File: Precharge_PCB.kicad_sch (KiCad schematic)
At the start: 74 parts, among them J1 Conn_01x02, J10 Conn_01x06, J2 Conn_01x02, J3 Conn_01x08, J4 Conn_01x02, J5 Conn_01x03, J9 Conn_01x02, K1 G2RL-1A, K2 G2RL-1A, Q1 DMN61D8LQ, Q2 DMN61D8LQ, SW2 SW_Push, U1 SN65HVD1050D, U2 TPS7B88, U3 STM32F103C8Tx, U4 MCP1700x-330xxMB, Y1 8M

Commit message: schematic: Assign all footprints
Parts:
- J3: footprint (none) -> yfs:MolexMicrofitPlus1x8
- JP1: footprint (none) -> Jumper:SolderJumper-2_P1.3mm_Open_TrianglePad1.0x1.5mm
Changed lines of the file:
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@@
 			)
 		)
-		(property "Footprint" ""
+		(property "Footprint" "yfs:MolexMicrofitPlus1x8"
 			(at 39.37 90.17 0)
 			(effects
@@
 			)
 		)
-		(property "Footprint" ""
+		(property "Footprint" "Jumper:SolderJumper-2_P1.3mm_Open_TrianglePad1.0x1.5mm"
 			(at 156.21 119.38 0)
 			(effects

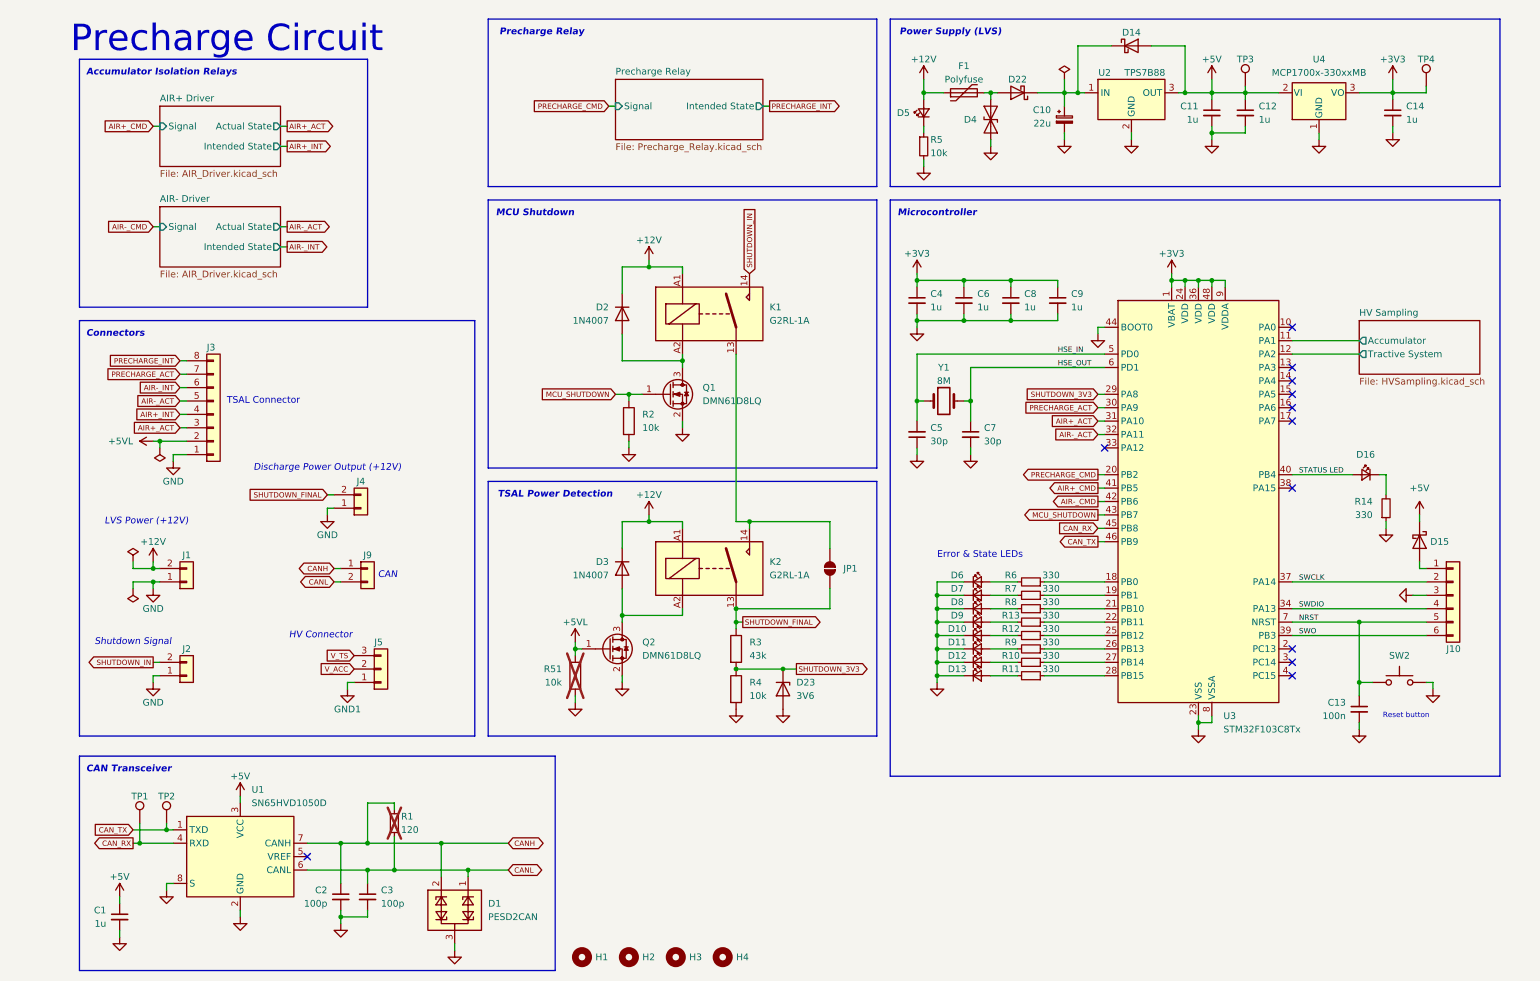
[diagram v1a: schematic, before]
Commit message: schematic: Reassign reference designators
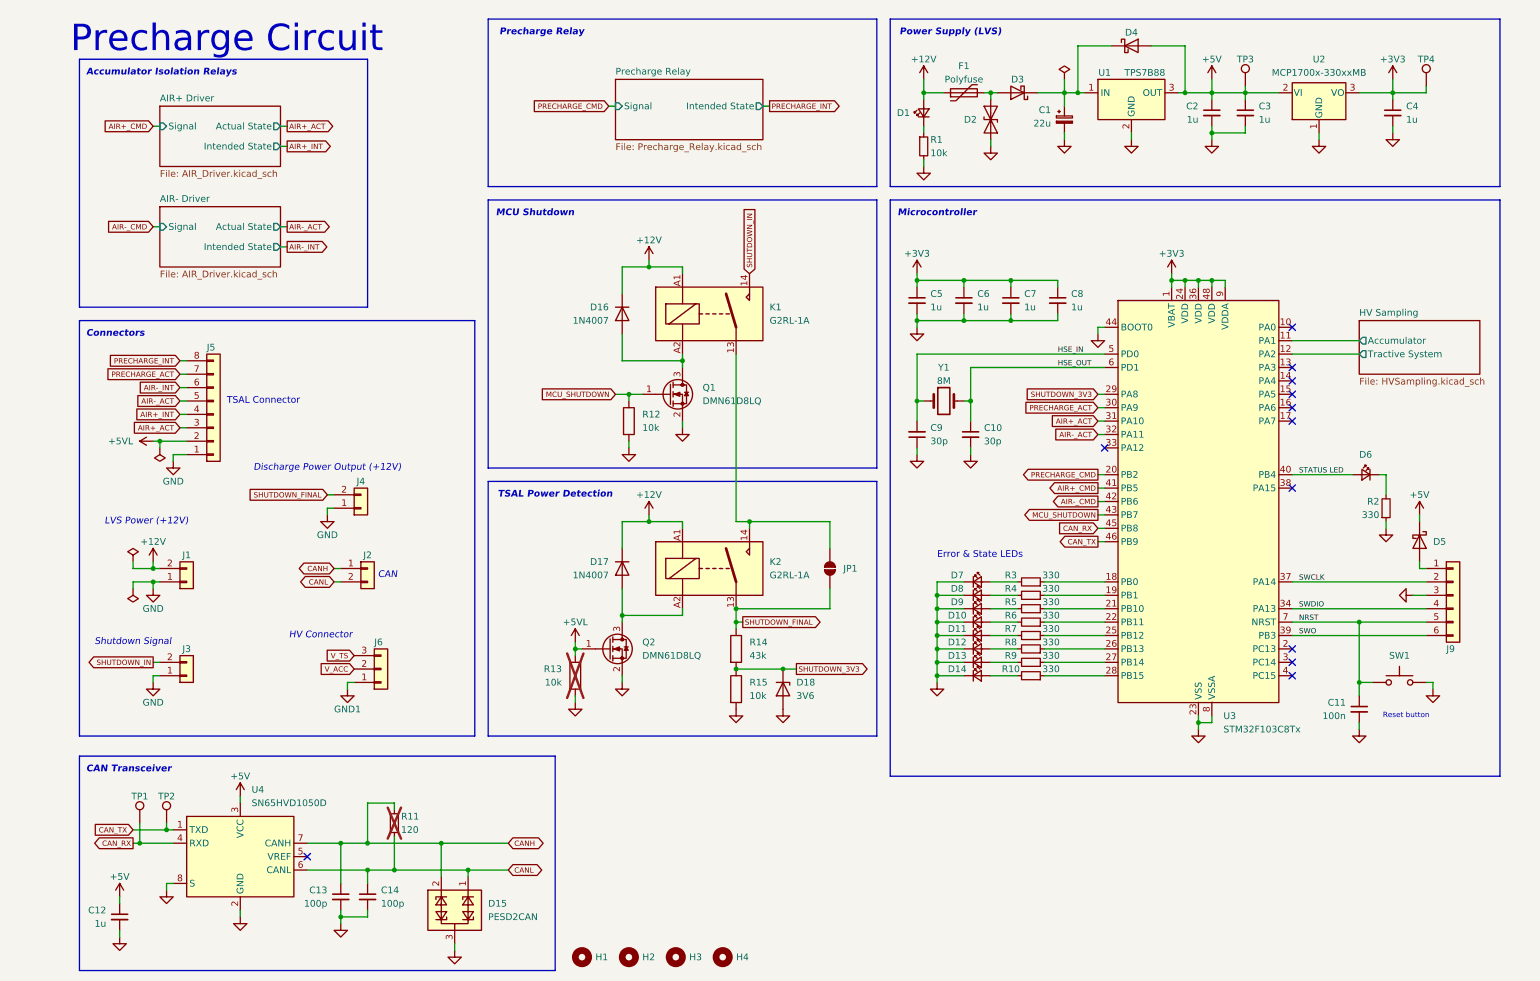
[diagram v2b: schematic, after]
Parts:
- renumbered C10 to C1, C7 to C10, C13 to C11, C1 to C12, C2 to C13, C3 to C14, C11 to C2, C12 to C3, C14 to C4, C4 to C5, C8 to C7, C9 to C8, C5 to C9, D5 to D1, D9 to D10, D10 to D11, D11 to D12, D12 to D13, D13 to D14, D1 to D15, D2 to D16, D3 to D17, D23 to D18, D4 to D2, D22 to D3, D14 to D4, D15 to D5, D16 to D6, D6 to D7, D7 to D8, D8 to D9, J9 to J2, J2 to J3, J3 to J5, J5 to J6, J10 to J9, R5 to R1, R11 to R10, R1 to R11, R2 to R12, R51 to R13, R3 to R14, R4 to R15, R14 to R2, R6 to R3, R7 to R4, R8 to R5, R13 to R6, R12 to R7, R9 to R8, R10 to R9, SW2 to SW1, U2 to U1, U4 to U2, U1 to U4

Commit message: schematic: Fill out most of the BOM
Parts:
- C13, C14: Dist (none) -> LCSC; Dist # (none) -> C126576; Mfr (none) -> Murata; Mfr # (none) -> GCM1885C2A101JA16D
- K1, K2: Dist (none) -> Mouser; Dist # (none) -> 653-G2RL-1A-DC12; Mfr (none) -> Omron; Mfr # (none) -> G2RL-1A-DC12
- Q1, Q2: Dist (none) -> LCSC; Dist # (none) -> C5248874; Mfr (none) -> DIODES; Mfr # (none) -> DMN61D8LQ-7
- R12, R13, R15: Dist (none) -> LCSC; Dist # (none) -> C25804; Mfr (none) -> Uni-Royal; Mfr # (none) -> 0603WAF1002T5E

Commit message: Revision A
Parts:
- added C31: 1u, Capacitor_SMD:C_0603_1608Metric, symbol Device:C_Small
- added F2: Polyfuse, Capacitor_SMD:C_0805_2012Metric, symbol Device:Polyfuse
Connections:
- net +3V3: now also C31.1
- net +5VL: now also F2.1; no longer J5.2 (Pin_2)
- net GND: now also D6.1 (K), C31.2; no longer R2.1
- net STATUS LED: now also R2.2; no longer D6.2 (A)
- new net: F2.2, J5.2 (Pin_2)
- new net: D6.2 (A), R2.1
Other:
- moved on the sheet: C10, C11, C5, C6, C7, C8, C9, D10, D11, D12, D13, D14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

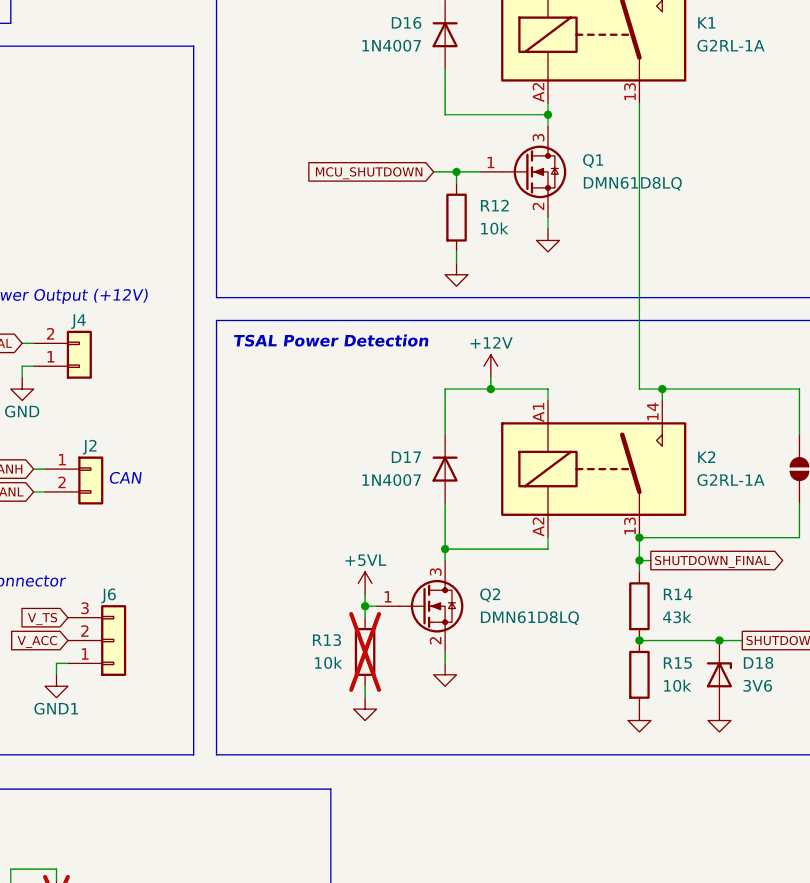
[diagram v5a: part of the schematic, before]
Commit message: *: Remove unnecessary MOSFET pull-downs
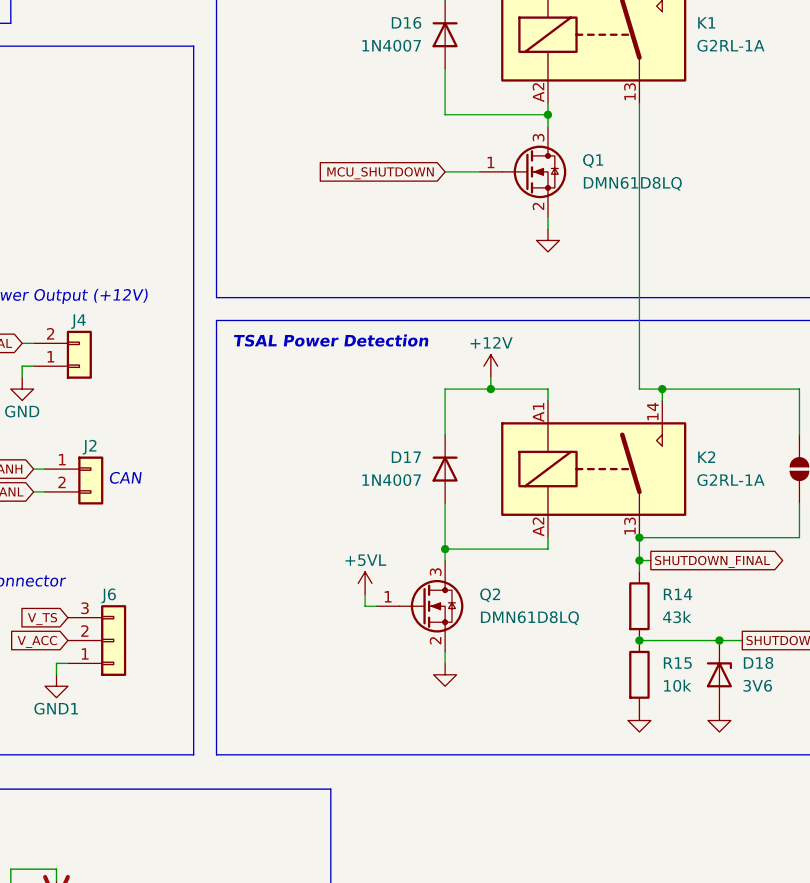
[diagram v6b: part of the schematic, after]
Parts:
- removed R12, R13: 10k, Resistor_SMD:R_0603_1608Metric, symbol Device:R

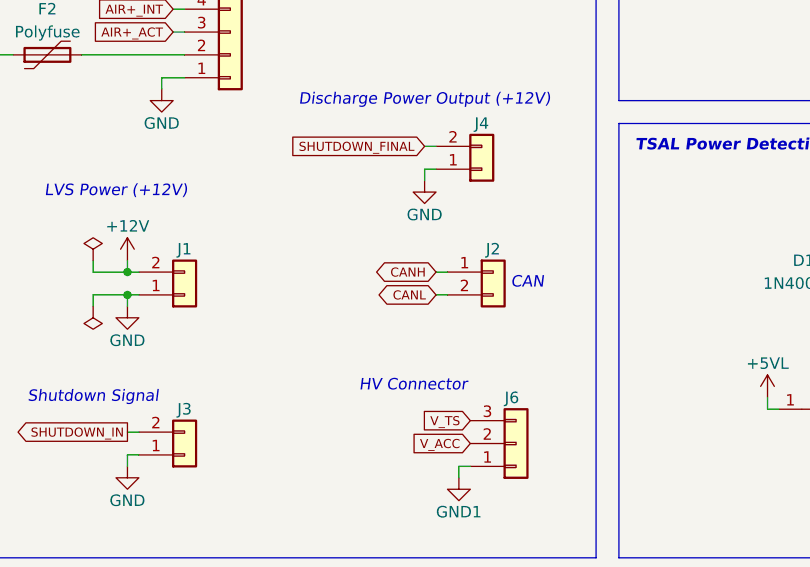
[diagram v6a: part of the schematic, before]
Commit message: Updated layout
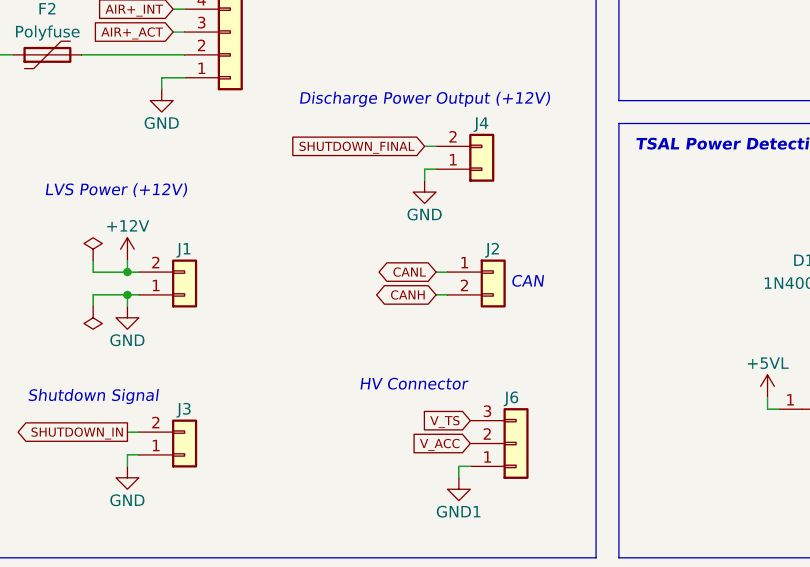
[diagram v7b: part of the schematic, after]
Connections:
- net CANH: now also J2.2 (Pin_2); no longer J2.1 (Pin_1)
- net CANL: now also J2.1 (Pin_1); no longer J2.2 (Pin_2)
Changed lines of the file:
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@@
 	(global_label "CANH"
 		(shape bidirectional)
-		(at 71.12 119.38 180)
-		(fields_autoplaced yes)
-		(effects
-			(font
-				(size 1 1)
-			)
-			(justify right)
-		)
-		(property "Intersheetrefs" "${INTERSHEET_REFS}"
-			(at 63.9424 119.38 0)
+		(at 71.12 121.92 180)
+		(fields_autoplaced yes)
+		(effects
+			(font
+				(size 1 1)
+			)
+			(justify right)
+		)
+		(property "Intersheetrefs" "${INTERSHEET_REFS}"
+			(at 63.9424 121.92 0)
 			(effects
 				(font
@@
 	(global_label "CANL"
 		(shape bidirectional)
-		(at 71.12 121.92 180)
-		(fields_autoplaced yes)
-		(effects
-			(font
-				(size 1 1)
-			)
-			(justify right)
-		)
-		(property "Intersheetrefs" "${INTERSHEET_REFS}"
-			(at 64.1805 121.92 0)
-			(effects
-				(font
+		(at 71.12 119.38 180)
+		(fields_autoplaced yes)
+		(effects
+			(font
+				(size 1 1)
+			)
+			(justify right)
+		)
+		(property "Intersheetrefs" "${INTERSHEET_REFS}"
+			(at 64.1805 119.38 0)
+			(effects
+				(font

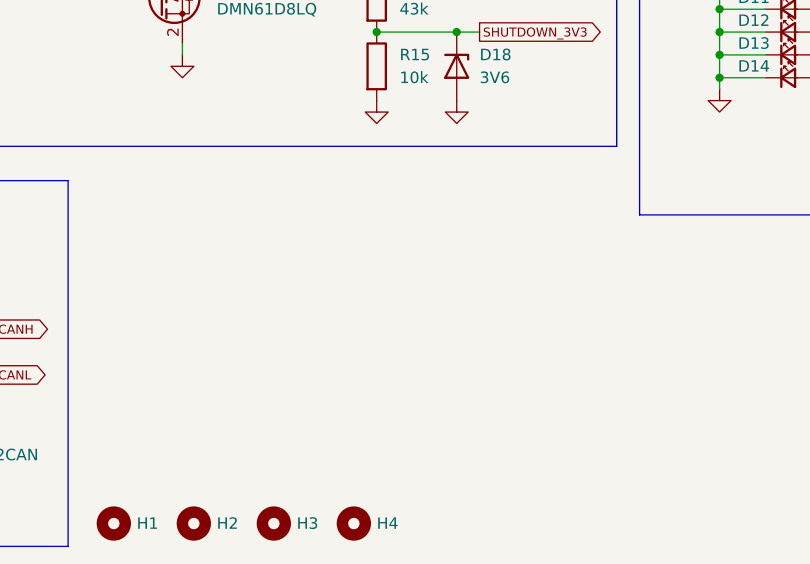
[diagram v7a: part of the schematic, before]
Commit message: *: Add +5V to +5VL jumper
This allows standalone precharge testing.
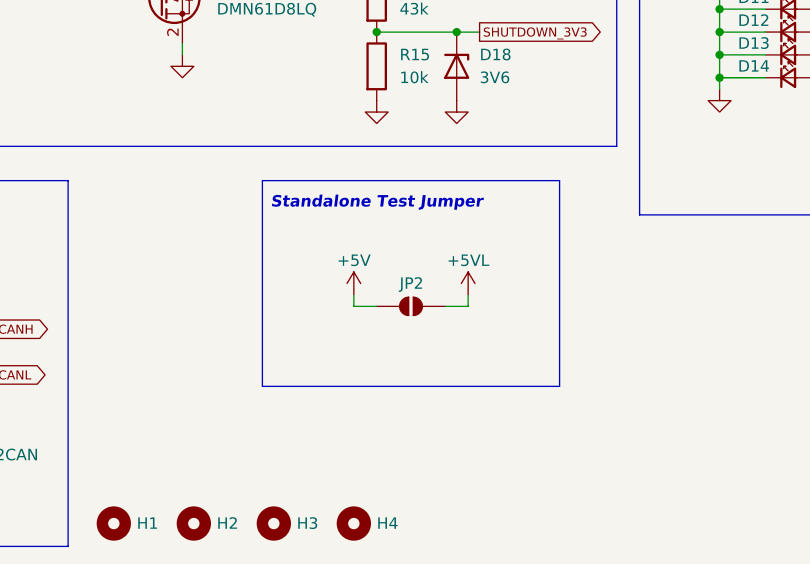
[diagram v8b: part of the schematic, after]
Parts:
- added JP2: SolderJumper_2_Open, Jumper:SolderJumper-2_P1.3mm_Open_TrianglePad1.0x1.5mm, symbol Jumper:SolderJumper_2_Open
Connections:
- net +5V: now also JP2.2 (B)
- net +5VL: now also JP2.1 (A)
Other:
- note added: "Standalone Test Jumper"
